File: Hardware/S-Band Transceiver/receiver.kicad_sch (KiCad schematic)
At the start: 69 parts, among them J6 SMA, J7 SMA, J8 SMA, U13 LT1819, U14 LT1819, U15 ADL5380, U16 TSS-53LNB3+, U17 SN74LVC1G125DCK, U18 SKY16603-632LF, U19 DCW-22-332+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

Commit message: Updating routing
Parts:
- R45: now fitted
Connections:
- net IQ_MIXER_EN: no longer names the net of R45.2, U15.7 (~{EN})
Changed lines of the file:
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@@
 	)
 	(junction
-		(at 81.28 66.04)
-		(diameter 0)
-		(color 0 0 0 0)
-	)
-	(junction
 		(at 54.61 58.42)
 		(diameter 0)
@@
 	(wire
 		(pts
-			(xy 81.28 66.04) (xy 81.28 60.96)
-		)
-		(stroke
-			(width 0)
-			(type default)
-		)
-	)
-	(wire
-		(pts
 			(xy 240.03 118.11) (xy 240.03 114.3)
 		)
@@
 	(wire
 		(pts
-			(xy 81.28 60.96) (xy 85.09 60.96)
-		)
-		(stroke
-			(width 0)
-			(type default)
-		)
-	)
-	(wire
-		(pts
 			(xy 106.68 82.55) (xy 104.14 82.55)
 		)
@@
 		)
 	)
-	(global_label "IQ_MIXER_EN"
-		(shape input)
-		(at 85.09 60.96 0)
-		(fields_autoplaced yes)
-		(effects
-			(font
-				(size 1.27 1.27)
-			)
-			(justify left)
-		)
-		(property "Intersheetrefs" "${INTERSHEET_REFS}"
-			(at 100.1099 60.96 0)
-			(effects
-				(font
-					(size 1.27 1.27)
-				)
-				(justify left)
-				(hide yes)
-			)
-		)
-	)
 	(global_label "RX_VRMS"
 		(shape input)
@@
 		(in_bom yes)
 		(on_board yes)
-		(dnp yes)
+		(dnp no)
 		(property "Reference" "R45"
 			(at 84.836 64.262 90)

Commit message: Updates to schematic
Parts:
- C79, C80, C83, C84, C85: value 10nF -> 10000pF
- J6, J7, J8: value SMA -> SMA-J-P-H-ST-EM1; Digikey (none) -> SAM8857-ND
- TR1: Digikey (none) -> 1465-1217-1-ND
- U13, U14: Digikey (none) -> LT1819CS8#TRPBFCT-ND
- U15: Digikey (none) -> 505-ADL5380ACPZ-R7CT-ND
- U16: Digikey (none) -> 3157-TSS-53LNB3+CT-ND
- U17: Digikey (none) -> 296-11604-1-ND
- U18: Digikey (none) -> 863-SKY16603-632LFCT-ND
- U19: Digikey (none) -> 3157-DCW-22-332+CT-ND
- U20: Digikey (none) -> 505-ADL5906ACPZN-R7CT-ND
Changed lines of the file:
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@@
 			)
 		)
+		(property "Digikey" "LT1819CS8#TRPBFCT-ND"
+			(at 121.92 33.02 0)
+			(effects
+				(font
+					(size 1.27 1.27)
+				)
+				(hide yes)
+			)
+		)
 		(pin "7"
 		)
@@
 			)
 		)
+		(property "Digikey" "3157-DCW-22-332+CT-ND"
+			(at 205.74 82.55 0)
+			(effects
+				(font
+					(size 1.27 1.27)
+				)
+				(hide yes)
+			)
+		)
 		(pin "4"
 		)
@@
 			)
 		)
-		(property "Value" "SMA"
+		(property "Value" "SMA-J-P-H-ST-EM1"
 			(at 153.67 34.5831 0)
 			(effects
@@
 			)
 		)
-		(property "Datasheet" " ~"
+		(property "Datasheet" "https://mm.digikey.com/Volume0/opasdata/d220001/medias/docus/6129/sma-j-p-x-st-em1-mkt.pdf"
 			(at 149.86 33.02 0)
 			(effects
@@
 			)
 		)
+		(property "Digikey" "SAM8857-ND"
+			(at 149.86 33.02 0)
+			(effects
+				(font
+					(size 1.27 1.27)
+				)
+				(hide yes)
+			)
+		)
 		(pin "1"
 		)
@@
 			)
 		)
-		(property "Value" "10nF"
+		(property "Value" "10000pF"
 			(at 227.3363 78.74 90)
 			(effects
@@
 			)
 		)
-		(property "Value" "SMA"
+		(property "Value" "SMA-J-P-H-ST-EM1"
 			(at 246.38 84.1131 0)
 			(effects
@@
 			)
 		)
-		(property "Datasheet" " ~"
+		(property "Datasheet" "https://mm.digikey.com/Volume0/opasdata/d220001/medias/docus/6129/sma-j-p-x-st-em1-mkt.pdf"
 			(at 242.57 82.55 0)
 			(effects
@@
 			)
 		)
+		(property "Digikey" "SAM8857-ND"
+			(at 242.57 82.55 0)
+			(effects
+				(font
+					(size 1.27 1.27)
+				)
+				(hide yes)
+			)
+		)
 		(pin "1"
 		)
@@
 			)
 		)
+		(property "Digikey" "1465-1217-1-ND"
+			(at 99.06 85.09 0)
+			(effects
+				(font
+					(size 1.27 1.27)
+				)
+				(hide yes)
+			)
+		)
 		(pin "5"
 		)
@@
 			)
 		)
+		(property "Digikey" "LT1819CS8#TRPBFCT-ND"
+			(at 100.33 30.48 0)
+			(effects
+				(font
+					(size 1.27 1.27)
+				)
+				(hide yes)
+			)
+		)
 		(pin "7"
 		)
@@
 			)
 		)
+		(property "Digikey" "505-ADL5380ACPZ-R7CT-ND"
+			(at 73.66 85.09 0)
+			(effects
+				(font
+					(size 1.27 1.27)
+				)
+				(hide yes)
+			)
+		)
 		(pin "25"
 		)
@@
 			)
 		)
+		(property "Digikey" "LT1819CS8#TRPBFCT-ND"
+			(at 111.76 129.54 0)
+			(effects
+				(font
+					(size 1.27 1.27)
+				)
+				(hide yes)
+			)
+		)
 		(pin "7"
 		)
@@
 			)
 		)
+		(property "Digikey" "LT1819CS8#TRPBFCT-ND"
+			(at 43.18 140.97 0)
+			(effects
+				(font
+					(size 1.27 1.27)
+				)
+				(hide yes)
+			)
+		)
 		(pin "7"
 		)
@@
 			)
 		)
+		(property "Digikey" "863-SKY16603-632LFCT-ND"
+			(at 168.91 82.55 0)
+			(effects
+				(font
+					(size 1.27 1.27)
+				)
+				(hide yes)
+			)
+		)
 		(pin "4"
 		)
@@
 			)
 		)
-		(property "Value" "SMA"
+		(property "Value" "SMA-J-P-H-ST-EM1"
 			(at 165.1 133.6431 0)
 			(effects
@@
 			)
 		)
-		(property "Datasheet" " ~"
+		(property "Datasheet" "https://mm.digikey.com/Volume0/opasdata/d220001/medias/docus/6129/sma-j-p-x-st-em1-mkt.pdf"
 			(at 161.29 132.08 0)
 			(effects
@@
 			)
 		)
+		(property "Digikey" "SAM8857-ND"
+			(at 161.29 132.08 0)
+			(effects
+				(font
+					(size 1.27 1.27)
+				)
+				(hide yes)
+			)
+		)
 		(pin "1"
 		)
@@
 			)
 		)
+		(property "Digikey" "3157-TSS-53LNB3+CT-ND"
+			(at 134.62 82.55 0)
+			(effects
+				(font
+					(size 1.27 1.27)
+				)
+				(hide yes)
+			)
+		)
 		(pin "8"
 		)
@@
 			)
 		)
-		(property "Value" "10nF"
+		(property "Value" "10000pF"
 			(at 90.17 90.424 90)
 			(effects
@@
 			)
 		)
+		(property "Digikey" "296-11604-1-ND"
+			(at 148.59 60.96 0)
+			(effects
+				(font
+					(size 1.27 1.27)
+				)
+				(hide yes)
+			)
+		)
 		(pin "1"
 		)
@@
 			)
 		)
+		(property "Digikey" "505-ADL5906ACPZN-R7CT-ND"
+			(at 240.03 134.62 0)
+			(effects
+				(font
+					(size 1.27 1.27)
+				)
+				(hide yes)
+			)
+		)
 		(pin "13"
 		)
@@
 			)
 		)
+		(property "Digikey" "LT1819CS8#TRPBFCT-ND"
+			(at 133.35 132.08 0)
+			(effects
+				(font
+					(size 1.27 1.27)
+				)
+				(hide yes)
+			)
+		)
 		(pin "7"
 		)
@@
 			)
 		)
-		(property "Value" "10nF"
+		(property "Value" "10000pF"
 			(at 223.5263 128.27 90)
 			(effects
@@
 			)
 		)
+		(property "Digikey" "LT1819CS8#TRPBFCT-ND"
+			(at 22.86 140.97 0)
+			(effects
+				(font
+					(size 1.27 1.27)
+				)
+				(hide yes)
+			)
+		)
 		(pin "7"
 		)
@@
 			)
 		)
-		(property "Value" "10nF"
+		(property "Value" "10000pF"
 			(at 220.98 143.5035 0)
 			(effects
@@
 			)
 		)
-		(property "Value" "10nF"
+		(property "Value" "10000pF"
 			(at 90.17 80.01 90)
 			(effects

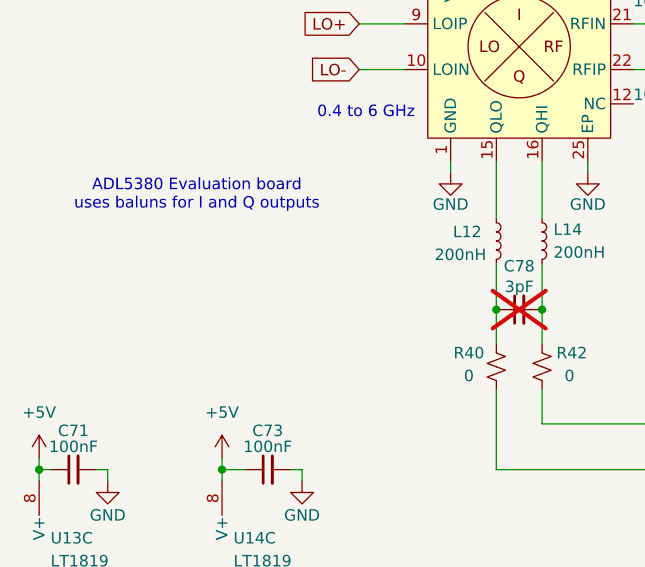
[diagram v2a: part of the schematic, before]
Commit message: Updating notes in schematic
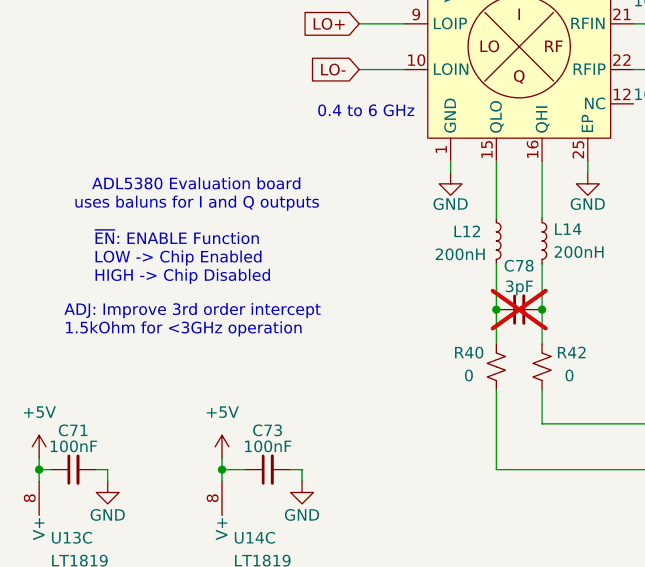
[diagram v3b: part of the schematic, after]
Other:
- note added: "ADJ: Improve 3rd order intercept 1.5kOhm for <3GHz operation"
- note added: "~{EN}: ENABLE Function LOW -> Chip Enabled HIGH -> Chip Disabled"
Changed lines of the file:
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@@
+		)
+	)
+	(text "~{EN}: ENABLE Function\nLOW -> Chip Enabled\nHIGH -> Chip Disabled"
+		(exclude_from_sim no)
+		(at 26.416 108.712 0)
+		(effects
+			(font
+				(size 1.27 1.27)
+			)
+			(justify left)
 		)
 	)
@@
 		)
 	)
+	(text "ADJ: Improve 3rd order intercept\n1.5kOhm for <3GHz operation"
+		(exclude_from_sim no)
+		(at 23.114 115.57 0)
+		(effects
+			(font
+				(size 1.27 1.27)
+			)
+			(justify left)
+		)
+	)

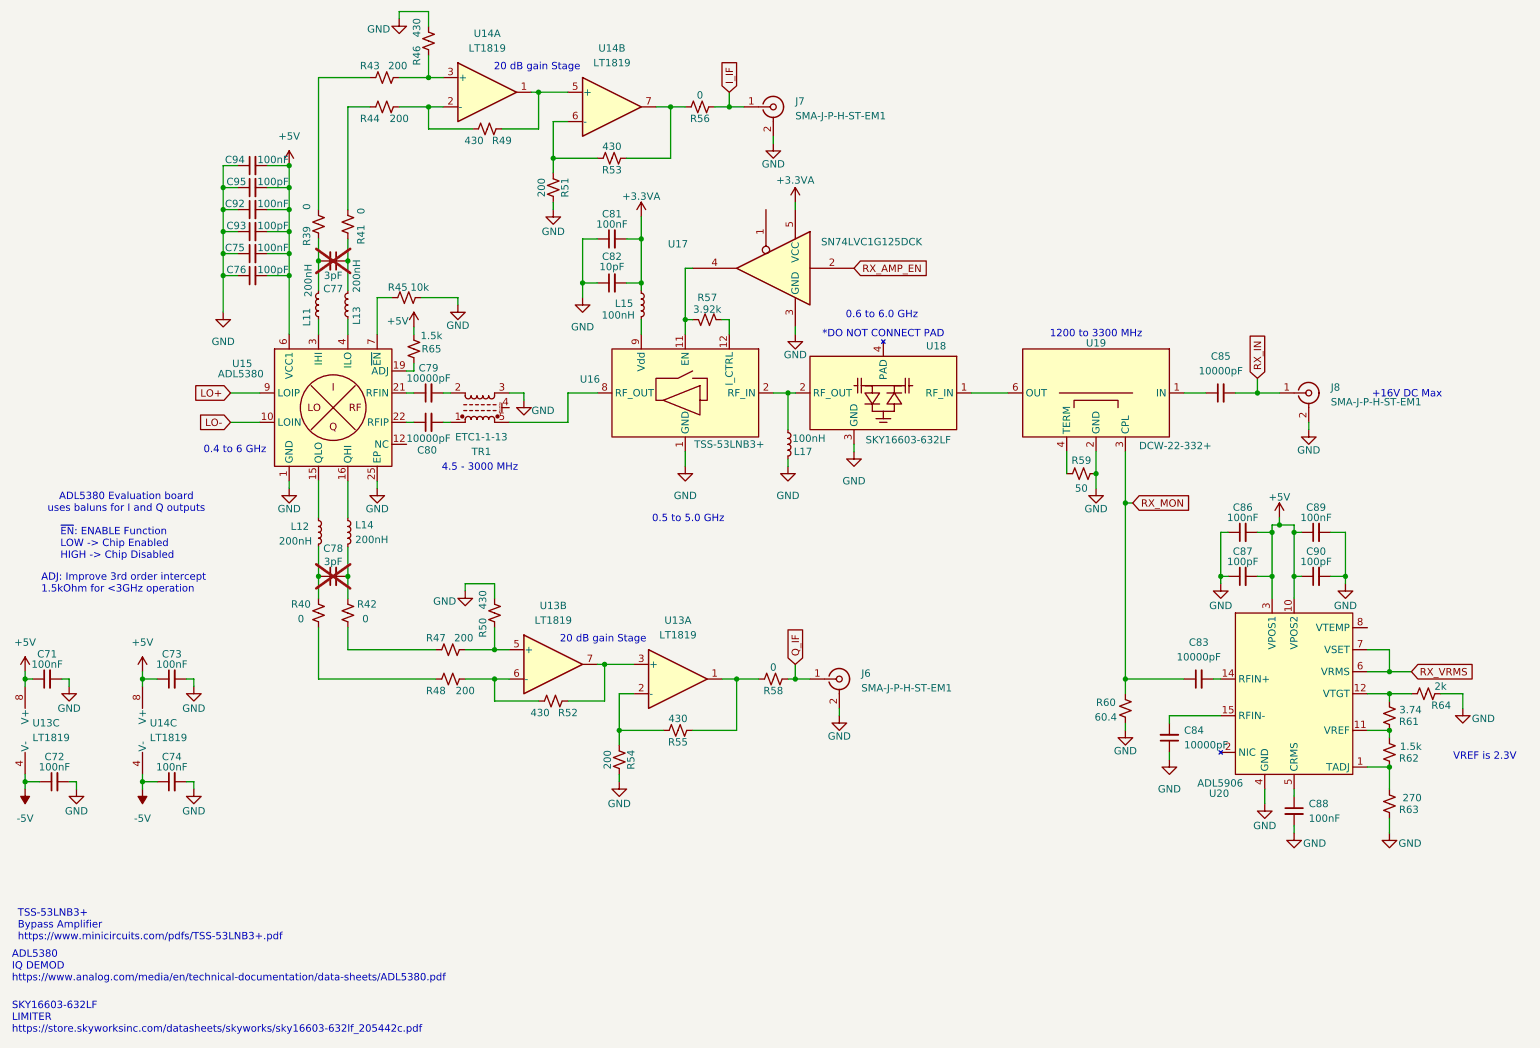
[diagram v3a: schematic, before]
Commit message: Updates to BOM
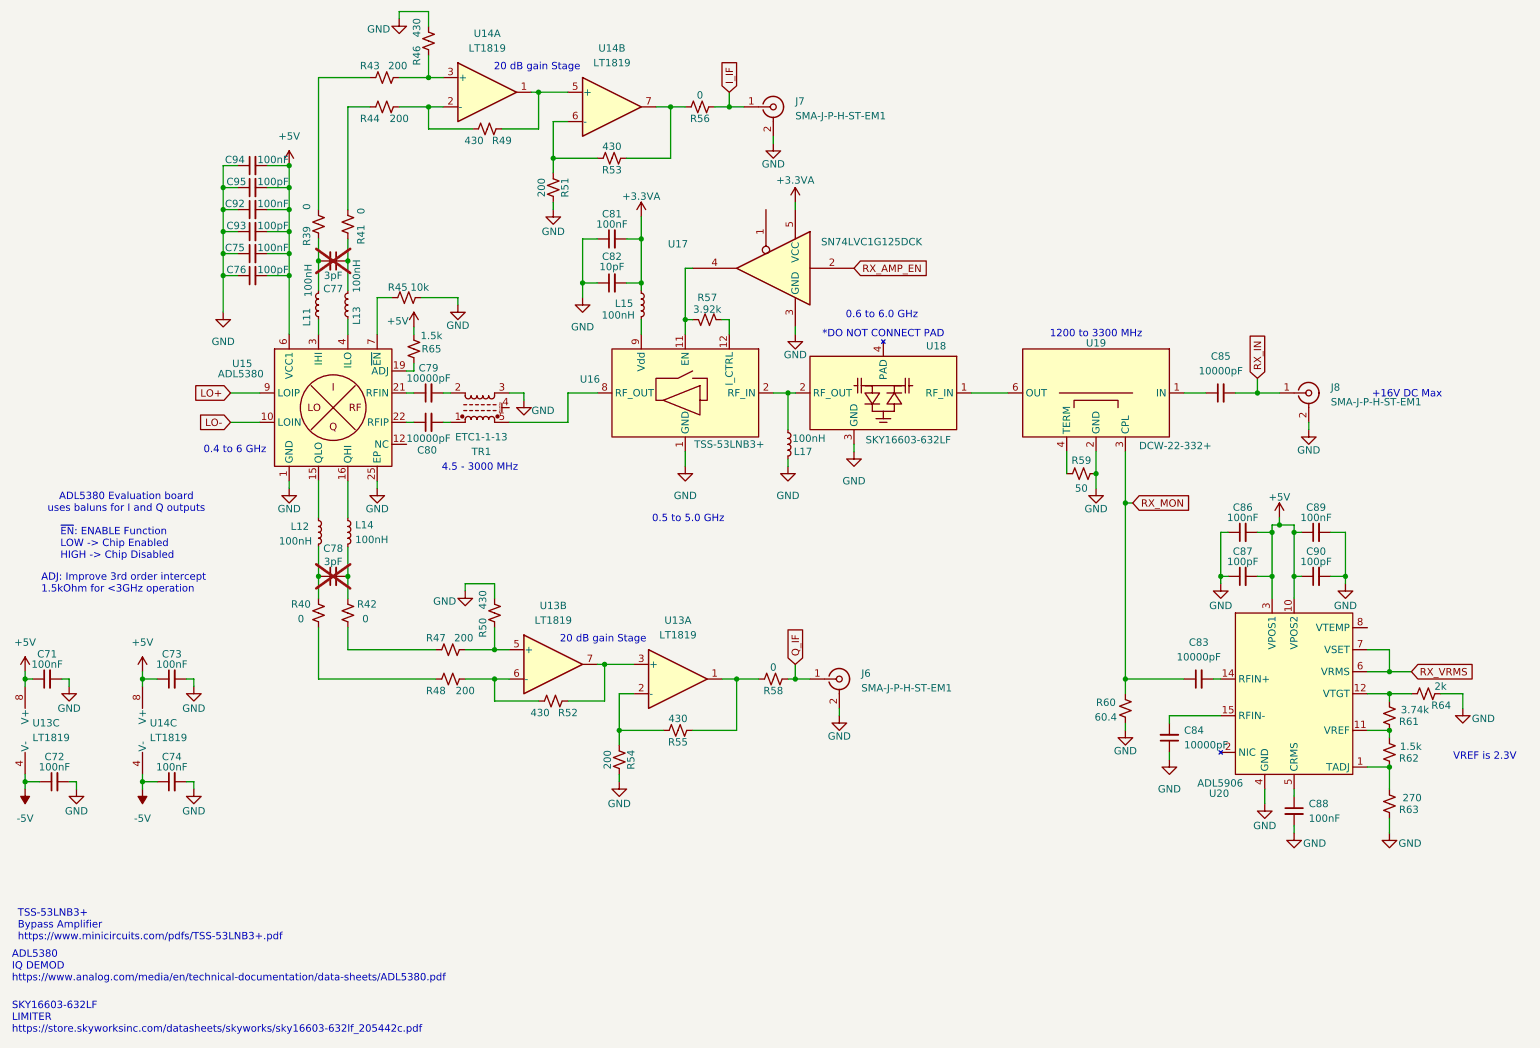
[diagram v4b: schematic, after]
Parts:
- L11, L12, L13, L14: value 200nH -> 100nH
- R61: value 3.74 -> 3.74k
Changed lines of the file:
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@@
 			)
 		)
-		(property "Value" "200nH"
+		(property "Value" "100nH"
 			(at 69.342 60.198 90)
 			(effects
@@
 			)
 		)
-		(property "Value" "200nH"
+		(property "Value" "100nH"
 			(at 64.262 108.204 0)
 			(effects
@@
 			)
 		)
-		(property "Value" "200nH"
+		(property "Value" "100nH"
 			(at 77.724 59.436 90)
 			(effects
@@
 			)
 		)
-		(property "Value" "3.74"
-			(at 262.128 137.414 0)
+		(property "Value" "3.74k"
+			(at 263.398 137.414 0)
 			(effects
 				(font
@@
 			)
 		)
-		(property "Value" "200nH"
+		(property "Value" "100nH"
 			(at 77.47 107.9499 0)
 			(effects

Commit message: Fixing issues in schematic
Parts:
- added R68: 1k, Resistor_SMD:R_0603_1608Metric, symbol Device:R_Small_US
- U17: value SN74LVC1G125DCK -> SN74LVC1G125DBVR
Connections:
- net GND: now also R68.2
- net at U17.1: now also R68.1
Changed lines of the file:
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@@
 	(wire
 		(pts
+			(xy 143.51 52.07) (xy 143.51 49.53)
+		)
+		(stroke
+			(width 0)
+			(type default)
+		)
+	)
+	(wire
+		(pts
 			(xy 149.86 82.55) (xy 152.4 82.55)
 		)
@@
 	(wire
 		(pts
+			(xy 148.59 49.53) (xy 148.59 50.8)
+		)
+		(stroke
+			(width 0)
+			(type default)
+		)
+	)
+	(wire
+		(pts
 			(xy 26.67 132.08) (xy 27.94 132.08)
 		)
@@
 	)
 	(symbol
+		(lib_id "power:GND")
+		(at 143.51 52.07 0)
+		(unit 1)
+		(exclude_from_sim no)
+		(in_bom yes)
+		(on_board yes)
+		(dnp no)
+		(property "Reference" "#PWR0143"
+			(at 143.51 58.42 0)
+			(effects
+				(font
+					(size 1.27 1.27)
+				)
+				(hide yes)
+			)
+		)
+		(property "Value" "GND"
+			(at 143.51 55.626 0)
+			(effects
+				(font
+					(size 1.27 1.27)
+				)
+			)
+		)
+		(property "Footprint" ""
+			(at 143.51 52.07 0)
+			(effects
+				(font
+					(size 1.27 1.27)
+				)
+				(hide yes)
+			)
+		)
+		(property "Datasheet" ""
+			(at 143.51 52.07 0)
+			(effects
+				(font
+					(size 1.27 1.27)
+				)
+				(hide yes)
+			)
+		)
+		(property "Description" "Power symbol creates a global label with name \"GND\" , ground"
+			(at 143.51 52.07 0)
+			(effects
+				(font
+					(size 1.27 1.27)
+				)
+				(hide yes)
+			)
+		)
+		(pin "1"
+		)
+		(instances
+			(project "S-Band Transceiver"
+				(path "/811f57cf-e3df-4fba-aff9-353adc85299e/f050a99f-ee17-49d7-ba1b-b225c3b6208d"
+					(reference "#PWR0143")
+					(unit 1)
+				)
+			)
+		)
+	)
+	(symbol
 		(lib_id "Device:R_Small_US")
 		(at 149.86 132.08 90)
@@
 	)
 	(symbol
+		(lib_id "Device:R_Small_US")
+		(at 146.05 49.53 270)
+		(unit 1)
+		(exclude_from_sim no)
+		(in_bom yes)
+		(on_board yes)
+		(dnp no)
+		(property "Reference" "R68"
+			(at 147.574 48.26 90)
+			(effects
+				(font
+					(size 1.27 1.27)
+				)
+				(justify left)
+			)
+		)
+		(property "Value" "1k"
+			(at 140.97 48.26 90)
+			(effects
+				(font
+					(size 1.27 1.27)
+				)
+				(justify left)
+			)
+		)
+		(property "Footprint" "Resistor_SMD:R_0603_1608Metric"
+			(at 146.05 49.53 0)
+			(effects
+				(font
+					(size 1.27 1.27)
+				)
+				(hide yes)
+			)
+		)
+		(property "Datasheet" "~"
+			(at 146.05 49.53 0)
+			(effects
+				(font
+					(size 1.27 1.27)
+				)
+				(hide yes)
+			)
+		)
+		(property "Description" "Resistor, small US symbol"
+			(at 146.05 49.53 0)
+			(effects
+				(font
+					(size 1.27 1.27)
+				)
+				(hide yes)
+			)
+		)
+		(pin "1"
+		)
+		(pin "2"
+		)
+		(instances
+			(project "S-Band Transceiver"
+				(path "/811f57cf-e3df-4fba-aff9-353adc85299e/f050a99f-ee17-49d7-ba1b-b225c3b6208d"
+					(reference "R68")
+					(unit 1)
+				)
+			)
+		)
+	)
+	(symbol
 		(lib_id "power:GND")
 		(at 152.4 95.25 0)
@@
 			)
 		)
-		(property "Value" "SN74LVC1G125DCK"
+		(property "Value" "SN74LVC1G125DBVR"
 			(at 166.878 56.388 0)
 			(effects

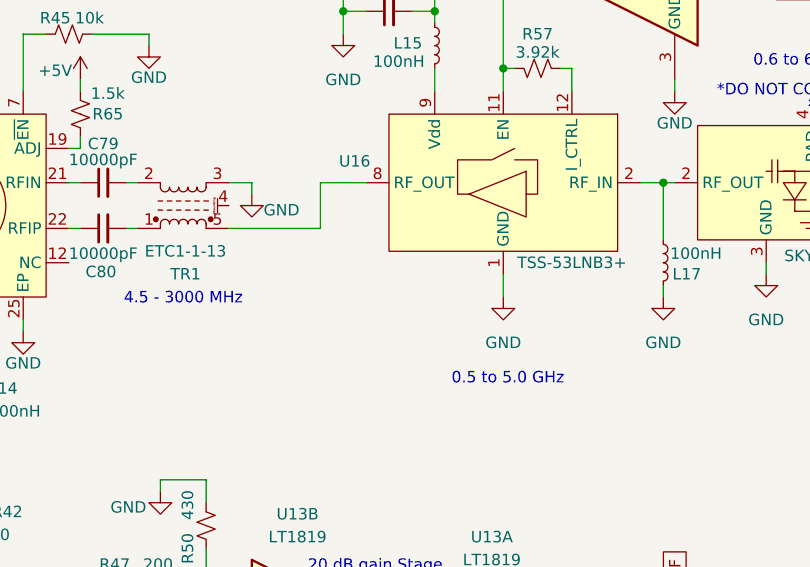
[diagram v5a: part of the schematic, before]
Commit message: Adding new script for tuning
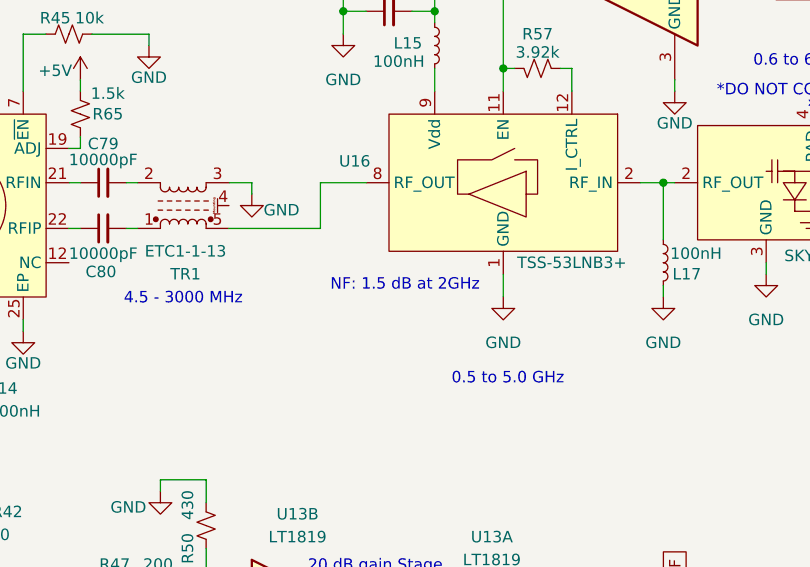
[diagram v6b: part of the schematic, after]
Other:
- note added: "NF: 1.5 dB at 2GHz"
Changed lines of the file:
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@@
+		)
+	)
+	(text "NF: 1.5 dB at 2GHz"
+		(exclude_from_sim no)
+		(at 123.698 93.98 0)
+		(effects
+			(font
+				(size 1.27 1.27)
+			)
 		)
 	)
